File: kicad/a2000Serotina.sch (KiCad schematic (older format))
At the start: 232 parts, among them J1 KCDX-5S-S2, U1 Teensy++2.0_(C)

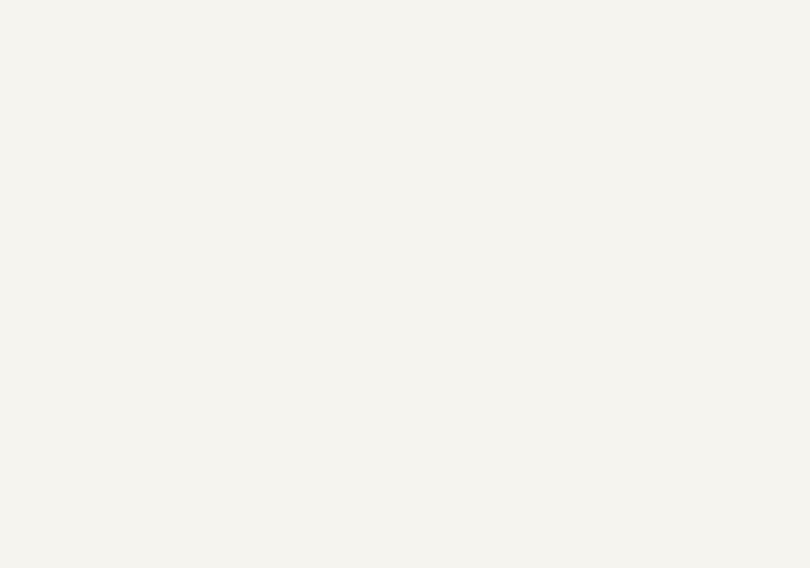
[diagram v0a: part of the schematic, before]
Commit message: Add Mounting holes
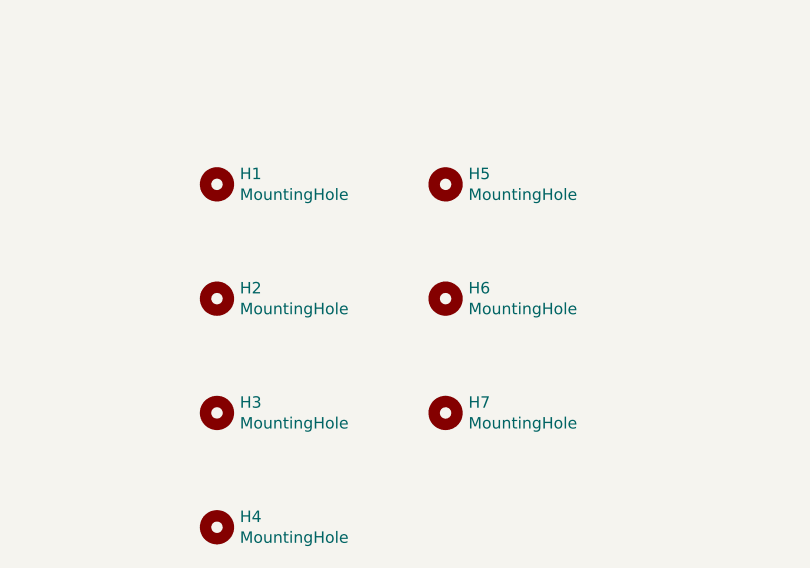
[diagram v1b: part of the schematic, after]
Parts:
- added H1, H2, H3, H4: MountingHole, MountingHole:MountingHole_2.2mm_M2, symbol Mechanical:MountingHole
- added H5, H6, H7: MountingHole, MountingHole:MountingHole_5.3mm_M5, symbol Mechanical:MountingHole
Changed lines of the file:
@@
 	5250 9050 7250 9050
 Connection ~ 5250 9050
+$Comp
+L Mechanical:MountingHole H1
+U 1 1 6108CB78
+P 11500 8500
+F 0 "H1" H 11600 8546 50  0000 L CNN
+F 1 "MountingHole" H 11600 8455 50  0000 L CNN
+F 2 "MountingHole:MountingHole_2.2mm_M2" H 11500 8500 50  0001 C CNN
+F 3 "~" H 11500 8500 50  0001 C CNN
+	1    11500 8500
+	1    0    0    -1
+$EndComp
+$Comp
+L Mechanical:MountingHole H2
+U 1 1 61091AB8
+P 11500 9000
+F 0 "H2" H 11600 9046 50  0000 L CNN
+F 1 "MountingHole" H 11600 8955 50  0000 L CNN
+F 2 "MountingHole:MountingHole_2.2mm_M2" H 11500 9000 50  0001 C CNN
+F 3 "~" H 11500 9000 50  0001 C CNN
+	1    11500 9000
+	1    0    0    -1
+$EndComp
+$Comp
+L Mechanical:MountingHole H3
+U 1 1 6109356F
+P 11500 9500
+F 0 "H3" H 11600 9546 50  0000 L CNN
+F 1 "MountingHole" H 11600 9455 50  0000 L CNN
+F 2 "MountingHole:MountingHole_2.2mm_M2" H 11500 9500 50  0001 C CNN
+F 3 "~" H 11500 9500 50  0001 C CNN
+	1    11500 9500
+	1    0    0    -1
+$EndComp
+$Comp
+L Mechanical:MountingHole H4
+U 1 1 61093A5D
+P 11500 10000
+F 0 "H4" H 11600 10046 50  0000 L CNN
+F 1 "MountingHole" H 11600 9955 50  0000 L CNN
+F 2 "MountingHole:MountingHole_2.2mm_M2" H 11500 10000 50  0001 C CNN
+F 3 "~" H 11500 10000 50  0001 C CNN
+	1    11500 10000
+	1    0    0    -1
+$EndComp
+$Comp
+L Mechanical:MountingHole H5
+U 1 1 610956B2
+P 12500 8500
+F 0 "H5" H 12600 8546 50  0000 L CNN
+F 1 "MountingHole" H 12600 8455 50  0000 L CNN
+F 2 "MountingHole:MountingHole_5.3mm_M5" H 12500 8500 50  0001 C CNN
+F 3 "~" H 12500 8500 50  0001 C CNN
+	1    12500 8500
+	1    0    0    -1
+$EndComp
+$Comp
+L Mechanical:MountingHole H6
+U 1 1 61095E33
+P 12500 9000
+F 0 "H6" H 12600 9046 50  0000 L CNN
+F 1 "MountingHole" H 12600 8955 50  0000 L CNN
+F 2 "MountingHole:MountingHole_5.3mm_M5" H 12500 9000 50  0001 C CNN
+F 3 "~" H 12500 9000 50  0001 C CNN
+	1    12500 9000
+	1    0    0    -1
+$EndComp
+$Comp
+L Mechanical:MountingHole H7
+U 1 1 6109789A
+P 12500 9500
+F 0 "H7" H 12600 9546 50  0000 L CNN
+F 1 "MountingHole" H 12600 9455 50  0000 L CNN
+F 2 "MountingHole:MountingHole_5.3mm_M5" H 12500 9500 50  0001 C CNN
+F 3 "~" H 12500 9500 50  0001 C CNN
+	1    12500 9500
+	1    0    0    -1
+$EndComp
 $EndSCHEMATC

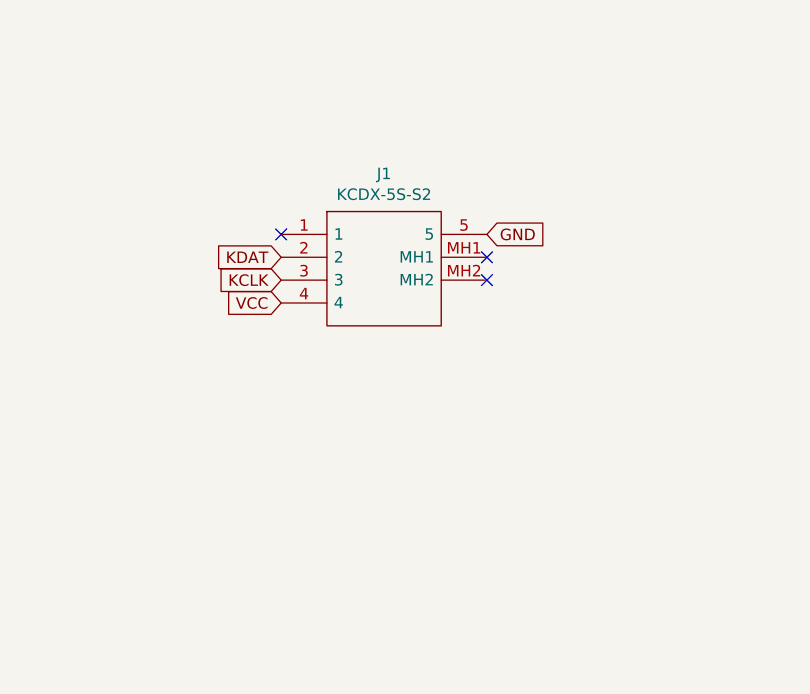
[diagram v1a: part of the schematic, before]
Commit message: Change 5 Pin Din to right angle pin headers
So that a case will fit on.
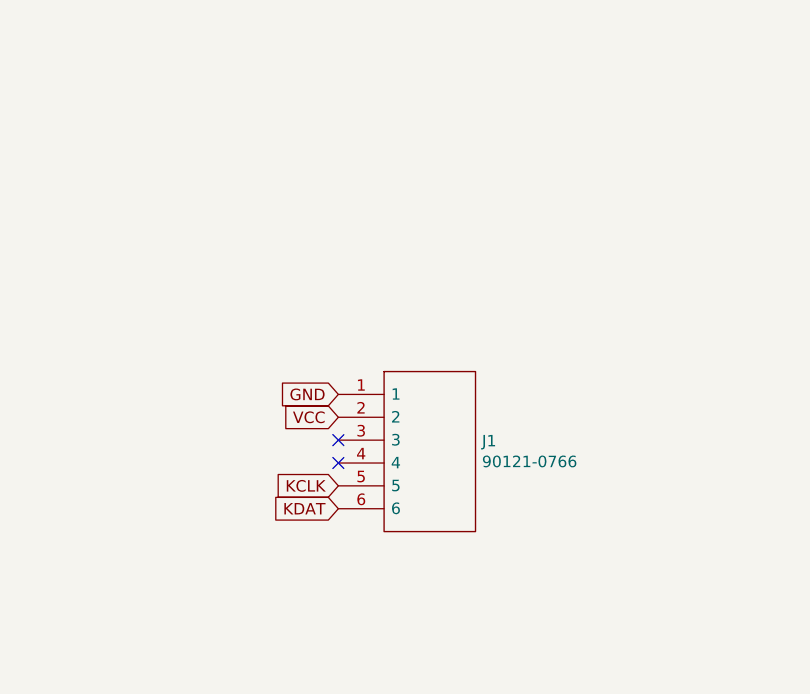
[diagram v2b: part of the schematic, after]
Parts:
- removed J1: KCDX-5S-S2, SamacSys_Parts:KCDX5SS2, symbol SamacSys_Parts:KCDX-5S-S2
- added J1: 90121-0766, SamacSys_Parts:901210766, symbol SamacSys_Parts:90121-0766
- H1, H2, H3, H4: footprint MountingHole:MountingHole_2.2mm_M2 -> MountingHole:MountingHole_3.2mm_M3
- H5, H6, H7: footprint MountingHole:MountingHole_5.3mm_M5 -> MountingHole:MountingHole_6.4mm_M6
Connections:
- net GND: now also J1.1
- net KCLK: now also J1.5
- net KDAT: now also J1.6
- net VCC: now also J1.2
- no-connect marks 21 -> 20
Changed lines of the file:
@@
 Wire Wire Line
 	7300 4650 7250 4650
-$Comp
-L SamacSys_Parts:KCDX-5S-S2 J1
-U 1 1 60E7B5EA
-P 12150 1950
-F 0 "J1" H 12600 2215 50  0000 C CNN
-F 1 "KCDX-5S-S2" H 12600 2124 50  0000 C CNN
-F 2 "SamacSys_Parts:KCDX5SS2" H 12900 2050 50  0001 L CNN
-F 3 "http://www.kycon.com/Pub_Eng_Draw/KCDX-5S-S2.pdf" H 12900 1950 50  0001 L CNN
-F 4 "Circular DIN Connectors 5P R/A PCB SHIELDED 5mm CIRC DIN RECPT" H 12900 1850 50  0001 L CNN "Description"
-F 5 "21.2" H 12900 1750 50  0001 L CNN "Height"
-F 6 "" H 12900 1650 50  0001 L CNN "Mouser Part Number"
-F 7 "" H 12900 1550 50  0001 L CNN "Mouser Price/Stock"
-F 8 "Kycon, Inc." H 12900 1450 50  0001 L CNN "Manufacturer_Name"
-F 9 "KCDX-5S-S2" H 12900 1350 50  0001 L CNN "Manufacturer_Part_Number"
-	1    12150 1950
-	1    0    0    -1
-$EndComp
-NoConn ~ 13050 2050
-NoConn ~ 13050 2150
-Text GLabel 13050 1950 2    50   Input ~ 0
-GND
-Text GLabel 12150 2250 0    50   Input ~ 0
+Text GLabel 12400 2650 0    50   Input ~ 0
+GND
+Text GLabel 12400 2750 0    50   Input ~ 0
 VCC
-Text GLabel 12150 2150 0    50   Input ~ 0
+Text GLabel 12400 3050 0    50   Input ~ 0
 KCLK
-Text GLabel 12150 2050 0    50   Input ~ 0
+Text GLabel 12400 3150 0    50   Input ~ 0
 KDAT
-NoConn ~ 12150 1950
 $Comp
 L Device:R_Small R1
@@
 F 0 "H1" H 11600 8546 50  0000 L CNN
 F 1 "MountingHole" H 11600 8455 50  0000 L CNN
-F 2 "MountingHole:MountingHole_2.2mm_M2" H 11500 8500 50  0001 C CNN
+F 2 "MountingHole:MountingHole_3.2mm_M3" H 11500 8500 50  0001 C CNN
 F 3 "~" H 11500 8500 50  0001 C CNN
 	1    11500 8500
@@
 F 0 "H2" H 11600 9046 50  0000 L CNN
 F 1 "MountingHole" H 11600 8955 50  0000 L CNN
-F 2 "MountingHole:MountingHole_2.2mm_M2" H 11500 9000 50  0001 C CNN
+F 2 "MountingHole:MountingHole_3.2mm_M3" H 11500 9000 50  0001 C CNN
 F 3 "~" H 11500 9000 50  0001 C CNN
 	1    11500 9000
@@
 F 0 "H3" H 11600 9546 50  0000 L CNN
 F 1 "MountingHole" H 11600 9455 50  0000 L CNN
-F 2 "MountingHole:MountingHole_2.2mm_M2" H 11500 9500 50  0001 C CNN
+F 2 "MountingHole:MountingHole_3.2mm_M3" H 11500 9500 50  0001 C CNN
 F 3 "~" H 11500 9500 50  0001 C CNN
 	1    11500 9500
@@
 F 0 "H4" H 11600 10046 50  0000 L CNN
 F 1 "MountingHole" H 11600 9955 50  0000 L CNN
-F 2 "MountingHole:MountingHole_2.2mm_M2" H 11500 10000 50  0001 C CNN
+F 2 "MountingHole:MountingHole_3.2mm_M3" H 11500 10000 50  0001 C CNN
 F 3 "~" H 11500 10000 50  0001 C CNN
 	1    11500 10000
@@
 F 0 "H5" H 12600 8546 50  0000 L CNN
 F 1 "MountingHole" H 12600 8455 50  0000 L CNN
-F 2 "MountingHole:MountingHole_5.3mm_M5" H 12500 8500 50  0001 C CNN
+F 2 "MountingHole:MountingHole_6.4mm_M6" H 12500 8500 50  0001 C CNN
 F 3 "~" H 12500 8500 50  0001 C CNN
 	1    12500 8500
@@
 F 0 "H6" H 12600 9046 50  0000 L CNN
 F 1 "MountingHole" H 12600 8955 50  0000 L CNN
-F 2 "MountingHole:MountingHole_5.3mm_M5" H 12500 9000 50  0001 C CNN
+F 2 "MountingHole:MountingHole_6.4mm_M6" H 12500 9000 50  0001 C CNN
 F 3 "~" H 12500 9000 50  0001 C CNN
 	1    12500 9000
@@
 F 0 "H7" H 12600 9546 50  0000 L CNN
 F 1 "MountingHole" H 12600 9455 50  0000 L CNN
-F 2 "MountingHole:MountingHole_5.3mm_M5" H 12500 9500 50  0001 C CNN
+F 2 "MountingHole:MountingHole_6.4mm_M6" H 12500 9500 50  0001 C CNN
 F 3 "~" H 12500 9500 50  0001 C CNN
 	1    12500 9500
 	1    0    0    -1
 $EndComp
+$Comp
+L SamacSys_Parts:90121-0766 J1
+U 1 1 610BC7F5
+P 12400 2650
+F 0 "J1" H 13028 2446 50  0000 L CNN
+F 1 "90121-0766" H 13028 2355 50  0000 L CNN
+F 2 "SamacSys_Parts:901210766" H 13050 2750 50  0001 L CNN
+F 3 "http://www.molex.com/webdocs/datasheets/pdf/en-us/0901210766_PCB_HEADERS.pdf" H 13050 2650 50  0001 L CNN
+F 4 "6 way single row r/a header Molex C-GRID III Series, Series Number 90121, 2.54mm Pitch 6 Way 1 Row Right Angle Pin Header, Through Hole" H 13050 2550 50  0001 L CNN "Description"
+F 5 "4" H 13050 2450 50  0001 L CNN "Height"
+F 6 "538-90121-0766" H 13050 2350 50  0001 L CNN "Mouser Part Number"
+F 7 "https://www.mouser.co.uk/ProductDetail/Molex/90121-0766?qs=PvP5v7EimslgD6hQyHQ2Ag%3D%3D" H 13050 2250 50  0001 L CNN "Mouser Price/Stock"
+F 8 "Molex" H 13050 2150 50  0001 L CNN "Manufacturer_Name"
+F 9 "90121-0766" H 13050 2050 50  0001 L CNN "Manufacturer_Part_Number"
+	1    12400 2650
+	1    0    0    -1
+$EndComp
+NoConn ~ 12400 2850
+NoConn ~ 12400 2950
 $EndSCHEMATC

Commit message: Updated PCB design, fitting into case
1) Add extra CTRL_LED in Right Ctrl Key  DONE

2) Add extra CAPS_LED in top right  LED6 R9 ( Previously KCLK )  DONE
CAPS_LOCK   NUM_LOCK    SCR_LOCK

3) Move NMLCK + SCLCK LEDs to top right  DONE

4) Fix font on second half of Thank you message  DONE
with thanks to LIV2 and Rob Taylor

5) Update Amiga keys on silkscreen  DONE

6) Move R12 to be in line with all other resistors  DONE

7) Need to move D72 so that it doesn't contact J1   DONE

8) Update Snip Silk screen  DONE

9) Move D3 - too close to MX Switch   DONE

10) Update firmware - add flash of all LEDs for 1.0s on start up...  DONE

12) Remove power LED   DONE

13) Remove KDAT + KCLK LEDS DONE

14) Move big Mounting holes H5, H6 + H7 right 1 square and up 1 square  DONE

15) Move H1 Up by 1mm  DONE

16) Move top row down. Should it be by 1 or 2 squares?  Try just one square   DONE

17) Make PCB wider so that it sits on the shelf properly

18) R10 + R11 missing   DONE
R12 -> R10
R13 -> R11
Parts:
- removed LED7, LED8: LED, LED_THT:LED_D3.0mm, symbol Device:LED
- removed MX12: MX-NoLED, MX_Alps_Hybrid:MX-1.25U-NoLED, symbol MX_Alps_Hybrid:MX-NoLED
- removed R10: 150, Resistor_THT:R_Axial_DIN0207_L6.3mm_D2.5mm_P10.16mm_Horizontal, symbol Device:R_Small
- added MX12: MX-LED, MX_Alps_Hybrid:MX-1.25U, symbol MX_Alps_Hybrid:MX-LED
- renumbered R12 to R10
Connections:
- net COL2: now also MX12.1 (COL)
- net CPLCK: now also R10.1, R9.1; no longer R10.2
- net GND: now also MX12.4 (LEDGND)
- net KCLK: no longer R9.1
- net VCC: no longer R11.1
- net at MX7.3 (LED): now also R10.2; no longer R10.1
- net at D12.2 (A): now also MX12.2 (ROW)
- net at R11.2: now also MX12.3 (LED)
- net LCTRL renamed CTRL
- net CTRL: now also R11.1
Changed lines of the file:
@@
 $EndComp
 Wire Wire Line
-	3300 9550 3250 9550
-$Comp
-L Device:D_Small D12
-U 1 1 60E65834
-P 3250 9650
-F 0 "D12" V 3250 9582 50  0000 R CNN
-F 1 "D_Small" V 3205 9582 50  0001 R CNN
-F 2 "Diode_THT:D_DO-35_SOD27_P7.62mm_Horizontal" V 3250 9650 50  0001 C CNN
-F 3 "~" V 3250 9650 50  0001 C CNN
-	1    3250 9650
-	0    -1   -1   0
-$EndComp
-$Comp
-L MX_Alps_Hybrid:MX-NoLED MX12
-U 1 1 60E6582E
-P 3350 9400
-F 0 "MX12" H 3383 9671 60  0000 C CNN
-F 1 "MX-NoLED" H 3383 9549 20  0001 C CNN
-F 2 "MX_Alps_Hybrid:MX-1.25U-NoLED" H 2725 9375 60  0001 C CNN
-F 3 "" H 2725 9375 60  0001 C CNN
-F 4 "RCTRL" H 3383 9573 50  0000 C CNN "Key"
-	1    3350 9400
-	1    0    0    -1
-$EndComp
-Wire Wire Line
 	2300 8850 2250 8850
 $Comp
@@
 $EndComp
 Text GLabel 2450 8900 2    50   Input ~ 0
-LCTRL
+CTRL
 $Comp
 L Device:R_Small R2
@@
 	12650 5950 12900 5950
 $Comp
-L Device:R_Small R9
-U 1 1 60FD484D
-P 13000 6300
-F 0 "R9" V 12804 6300 50  0000 C CNN
-F 1 "150" V 12895 6300 50  0000 C CNN
-F 2 "Resistor_THT:R_Axial_DIN0207_L6.3mm_D2.5mm_P10.16mm_Horizontal" H 13000 6300 50  0001 C CNN
-F 3 "~" H 13000 6300 50  0001 C CNN
-	1    13000 6300
-	0    1    1    0
-$EndComp
-Text GLabel 13100 6300 2    50   Input ~ 0
-KCLK
-$Comp
-L Device:LED LED6
-U 1 1 60FD4854
-P 12500 6300
-F 0 "LED6" H 12493 6425 50  0000 C CNN
-F 1 "LED" H 12493 6425 50  0001 C CNN
-F 2 "LED_THT:LED_D3.0mm" H 12500 6300 50  0001 C CNN
-F 3 "~" H 12500 6300 50  0001 C CNN
-	1    12500 6300
-	1    0    0    -1
-$EndComp
-Text GLabel 12350 6300 0    50   Input ~ 0
-GND
-Wire Wire Line
-	12650 6300 12900 6300
-$Comp
 L Device:R_Small R10
-U 1 1 60FF3D67
-P 13000 6650
-F 0 "R10" V 12804 6650 50  0000 C CNN
-F 1 "150" V 12895 6650 50  0000 C CNN
-F 2 "Resistor_THT:R_Axial_DIN0207_L6.3mm_D2.5mm_P10.16mm_Horizontal" H 13000 6650 50  0001 C CNN
-F 3 "~" H 13000 6650 50  0001 C CNN
-	1    13000 6650
-	0    1    1    0
-$EndComp
-Text GLabel 13100 6650 2    50   Input ~ 0
-KDAT
-$Comp
-L Device:LED LED7
-U 1 1 60FF3D6E
-P 12500 6650
-F 0 "LED7" H 12493 6775 50  0000 C CNN
-F 1 "LED" H 12493 6775 50  0001 C CNN
-F 2 "LED_THT:LED_D3.0mm" H 12500 6650 50  0001 C CNN
-F 3 "~" H 12500 6650 50  0001 C CNN
-	1    12500 6650
-	1    0    0    -1
-$EndComp
-Text GLabel 12350 6650 0    50   Input ~ 0
-GND
-Wire Wire Line
-	12650 6650 12900 6650
-$Comp
-L Device:R_Small R11
-U 1 1 61012FC1
-P 13000 7000
-F 0 "R11" V 12804 7000 50  0000 C CNN
-F 1 "150" V 12895 7000 50  0000 C CNN
-F 2 "Resistor_THT:R_Axial_DIN0207_L6.3mm_D2.5mm_P10.16mm_Horizontal" H 13000 7000 50  0001 C CNN
-F 3 "~" H 13000 7000 50  0001 C CNN
-	1    13000 7000
-	0    1    1    0
-$EndComp
-Text GLabel 13100 7000 2    50   Input ~ 0
-VCC
-$Comp
-L Device:LED LED8
-U 1 1 61012FC8
-P 12500 7000
-F 0 "LED8" H 12493 7125 50  0000 C CNN
-F 1 "LED" H 12493 7125 50  0001 C CNN
-F 2 "LED_THT:LED_D3.0mm" H 12500 7000 50  0001 C CNN
-F 3 "~" H 12500 7000 50  0001 C CNN
-	1    12500 7000
-	1    0    0    -1
-$EndComp
-Text GLabel 12350 7000 0    50   Input ~ 0
-GND
-Wire Wire Line
-	12650 7000 12900 7000
-$Comp
-L Device:R_Small R12
 U 1 1 610519E9
 P 2450 6000
-F 0 "R12" H 2509 6046 50  0000 L CNN
+F 0 "R10" H 2509 6046 50  0000 L CNN
 F 1 "150" H 2509 5955 50  0000 L CNN
 F 2 "Resistor_THT:R_Axial_DIN0207_L6.3mm_D2.5mm_P10.16mm_Horizontal" H 2450 6000 50  0001 C CNN
 F 3 "~" H 2450 6000 50  0001 C CNN
 	1    2450 6000
-	1    0    0    -1
+	-1   0    0    1
 $EndComp
 Text GLabel 2100 6100 0    50   Input ~ 0
@@
 RGUI
 Text GLabel 18300 2900 0    50   Input ~ 0
-LCTRL
+CTRL
 Text GLabel 18300 3000 0    50   Input ~ 0
 LALT
@@
 Text GLabel 2350 6000 3    50   Input ~ 0
 GND
-$Comp
-L MX_Alps_Hybrid:MX-LED MX7
-U 1 1 60E5D07F
-P 2350 5900
-F 0 "MX7" H 2432 6172 60  0000 C CNN
-F 1 "MX-LED" H 2432 6050 20  0001 C CNN
-F 2 "MX_Alps_Hybrid:MX-1.75U" H 1725 5875 60  0001 C CNN
-F 3 "" H 1725 5875 60  0001 C CNN
-F 4 "CAPS" H 2432 6074 50  0000 C CNN "Key"
-	1    2350 5900
-	1    0    0    -1
-$EndComp
 Wire Wire Line
 	2100 6100 2450 6100
@@
 Connection ~ 3250 9050
 Wire Wire Line
-	2750 9750 3250 9750
-Wire Wire Line
-	3250 9750 3750 9750
-Connection ~ 3250 9750
-Wire Wire Line
 	3750 9750 4250 9750
-Connection ~ 3750 9750
 Wire Wire Line
 	4250 9750 4750 9750
@@
 	2500 4450 2500 5150
 Connection ~ 2500 4450
-Wire Wire Line
-	2500 5150 2500 5850
 Connection ~ 2500 5150
 Wire Wire Line
-	2500 5850 2500 6550
-Connection ~ 2500 5850
-Wire Wire Line
 	2500 6550 2500 7250
 Connection ~ 2500 6550
@@
 Connection ~ 3500 7250
 Wire Wire Line
-	3500 8650 3500 9350
-Connection ~ 3500 8650
-Wire Wire Line
 	4000 1350 4000 1650
 Wire Wire Line
@@
 	2250 9750 2750 9750
 Connection ~ 2250 9750
-Connection ~ 2750 9750
 Wire Wire Line
 	2500 8650 2500 9350
@@
 NoConn ~ 12400 2850
 NoConn ~ 12400 2950
+Wire Wire Line
+	3300 9550 3250 9550
+$Comp
+L Device:D_Small D12
+U 1 1 6122EF07
+P 3250 9650
+F 0 "D12" V 3250 9582 50  0000 R CNN
+F 1 "D_Small" V 3205 9582 50  0001 R CNN
+F 2 "Diode_THT:D_DO-35_SOD27_P7.62mm_Horizontal" V 3250 9650 50  0001 C CNN
+F 3 "~" V 3250 9650 50  0001 C CNN
+	1    3250 9650
+	0    -1   -1   0
+$EndComp
+$Comp
+L Device:R_Small R11
+U 1 1 6122EF0D
+P 3450 9500
+F 0 "R11" V 3254 9500 50  0000 C CNN
+F 1 "150" V 3345 9500 50  0000 C CNN
+F 2 "Resistor_THT:R_Axial_DIN0207_L6.3mm_D2.5mm_P10.16mm_Horizontal" H 3450 9500 50  0001 C CNN
+F 3 "~" H 3450 9500 50  0001 C CNN
+	1    3450 9500
+	-1   0    0    1
+$EndComp
+Text GLabel 3450 9600 3    50   Input ~ 0
+CTRL
+$Comp
+L MX_Alps_Hybrid:MX-LED MX12
+U 1 1 6122EF15
+P 3350 9400
+F 0 "MX12" H 3432 9672 60  0000 C CNN
+F 1 "MX-LED" H 3432 9550 20  0001 C CNN
+F 2 "MX_Alps_Hybrid:MX-1.25U" H 2725 9375 60  0001 C CNN
+F 3 "" H 2725 9375 60  0001 C CNN
+F 4 "RCTRL" H 3432 9574 50  0000 C CNN "Key"
+	1    3350 9400
+	1    0    0    -1
+$EndComp
+Text GLabel 3350 9500 3    50   Input ~ 0
+GND
+Wire Wire Line
+	3500 8650 3500 9350
+Connection ~ 3500 8650
+Wire Wire Line
+	2750 9750 3250 9750
+Connection ~ 2750 9750
+Wire Wire Line
+	3250 9750 3750 9750
+Connection ~ 3250 9750
+Connection ~ 3750 9750
+Wire Wire Line
+	12650 6300 12900 6300
+Text GLabel 12350 6300 0    50   Input ~ 0
+GND
+$Comp
+L Device:LED LED6
+U 1 1 60FD4854
+P 12500 6300
+F 0 "LED6" H 12493 6425 50  0000 C CNN
+F 1 "LED" H 12493 6425 50  0001 C CNN
+F 2 "LED_THT:LED_D3.0mm" H 12500 6300 50  0001 C CNN
+F 3 "~" H 12500 6300 50  0001 C CNN
+	1    12500 6300
+	1    0    0    -1
+$EndComp
+Text GLabel 13100 6300 2    50   Input ~ 0
+CPLCK
+$Comp
+L Device:R_Small R9
+U 1 1 60FD484D
+P 13000 6300
+F 0 "R9" V 12804 6300 50  0000 C CNN
+F 1 "150" V 12895 6300 50  0000 C CNN
+F 2 "Resistor_THT:R_Axial_DIN0207_L6.3mm_D2.5mm_P10.16mm_Horizontal" H 13000 6300 50  0001 C CNN
+F 3 "~" H 13000 6300 50  0001 C CNN
+	1    13000 6300
+	0    1    1    0
+$EndComp
+Connection ~ 2500 5850
+Wire Wire Line
+	2500 5850 2500 6550
+Wire Wire Line
+	2500 5150 2500 5850
+$Comp
+L MX_Alps_Hybrid:MX-LED MX7
+U 1 1 60E5D07F
+P 2350 5900
+F 0 "MX7" H 2432 6172 60  0000 C CNN
+F 1 "MX-LED" H 2432 6050 20  0001 C CNN
+F 2 "MX_Alps_Hybrid:MX-1.75U" H 1725 5875 60  0001 C CNN
+F 3 "" H 1725 5875 60  0001 C CNN
+F 4 "CAPS" H 2432 6074 50  0000 C CNN "Key"
+	1    2350 5900
+	1    0    0    -1
+$EndComp
 $EndSCHEMATC
